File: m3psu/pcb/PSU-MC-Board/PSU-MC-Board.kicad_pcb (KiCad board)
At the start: 2 copper layers, 40 x 40 mm, 60 parts, among them IC1 STM32F405RxTx, IC2 TPS62152, IC3 MCP2562, IC4 LTC4353, IC5 LTC4151, J1 WEST TOP, J2 WEST BOT, J3 NORTH TOP, J4 EAST TOP, J5 EAST BOT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

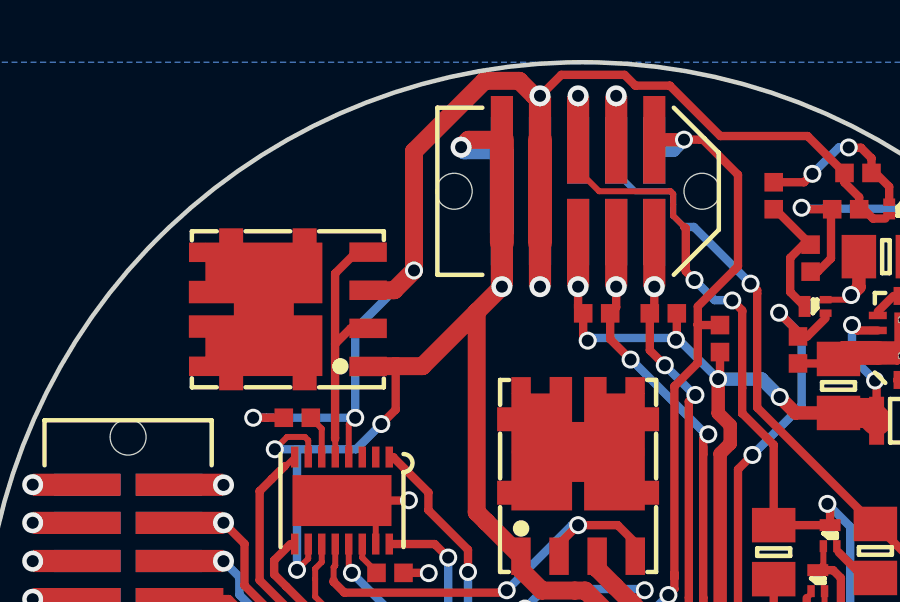
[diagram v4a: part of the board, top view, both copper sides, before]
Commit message: Modified DC-DC board routing to hopefully better performance.
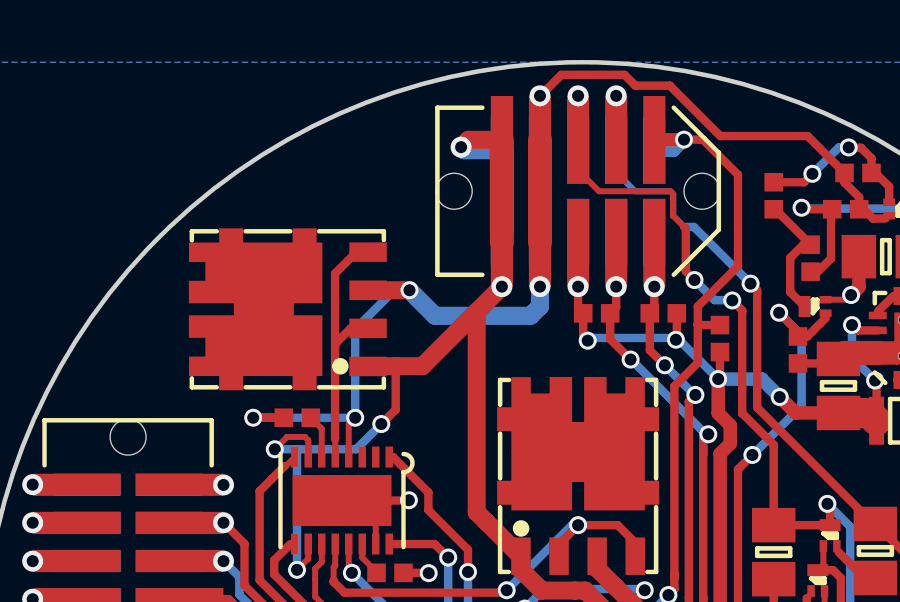
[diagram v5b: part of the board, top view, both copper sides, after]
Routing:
- net VBATT: track 49.6 -> 44.9 mm
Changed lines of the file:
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@@
     (links 240)
     (no_connects 0)
-    (area 80.074999 80.124999 120.225001 120.275001)
+    (area 79.75 79.25 120.225001 120.495)
     (thickness 1.6)
     (drawings 1)
-    (tracks 1171)
+    (tracks 1170)
     (zones 0)
     (modules 60)
@@
   )
   (setup
-    (last_trace_width 0.28)
+    (last_trace_width 0.45)
     (user_trace_width 0.2)
     (user_trace_width 0.28)
@@
   (segment (start 91.455 93.36) (end 91.455 92.415) (width 0.2) (layer F.Cu) (net 13))
   (segment (start 91.455 92.415) (end 91.09 92.05) (width 0.2) (layer F.Cu) (net 13))
-  (via (at 94.53 87.14) (size 0.6) (drill 0.4) (layers F.Cu B.Cu) (net 14))
-  (segment (start 92.57 92.05) (end 92.57 89.1) (width 0.28) (layer B.Cu) (net 14))
-  (segment (start 92.57 89.1) (end 94.53 87.14) (width 0.28) (layer B.Cu) (net 14))
+  (segment (start 94.38 87.8) (end 93.87 87.8) (width 0.28) (layer B.Cu) (net 14))
+  (segment (start 92.57 89.1) (end 92.57 92.05) (width 0.28) (layer B.Cu) (net 14))
+  (segment (start 93.87 87.8) (end 92.57 89.1) (width 0.28) (layer B.Cu) (net 14))
+  (segment (start 98.73 87.68) (end 98.73 88.34) (width 0.6) (layer B.Cu) (net 14))
+  (segment (start 94.38 87.8) (end 93 87.8) (width 0.6) (layer F.Cu) (net 14))
+  (via (at 94.38 87.8) (size 0.6) (drill 0.4) (layers F.Cu B.Cu) (net 14))
+  (segment (start 95.23 88.65) (end 94.38 87.8) (width 0.6) (layer B.Cu) (net 14))
+  (segment (start 98.42 88.65) (end 95.23 88.65) (width 0.6) (layer B.Cu) (net 14))
+  (segment (start 98.73 88.34) (end 98.42 88.65) (width 0.6) (layer B.Cu) (net 14))
   (segment (start 92.355 93.36) (end 92.355 92.265) (width 0.2) (layer F.Cu) (net 14))
-  (segment (start 92.57 92.05) (end 89.62 92.05) (width 0.28) (layer B.Cu) (net 14))
-  (via (at 92.57 92.05) (size 0.6) (drill 0.4) (layers F.Cu B.Cu) (net 14))
   (segment (start 92.355 92.265) (end 92.57 92.05) (width 0.2) (layer F.Cu) (net 14))
-  (segment (start 90.19 92.05) (end 89.17 92.05) (width 0.28) (layer F.Cu) (net 14))
-  (via (at 89.17 92.05) (size 0.6) (drill 0.4) (layers F.Cu B.Cu) (net 14))
+  (via (at 92.57 92.05) (size 0.6) (drill 0.4) (layers F.Cu B.Cu) (net 14))
+  (segment (start 92.57 92.05) (end 89.62 92.05) (width 0.28) (layer B.Cu) (net 14))
   (segment (start 89.62 92.05) (end 89.17 92.05) (width 0.28) (layer B.Cu) (net 14))
-  (segment (start 98.73 81.32) (end 98.54 81.32) (width 0.6) (layer F.Cu) (net 14))
-  (segment (start 94.53 83.17) (end 94.53 87.14) (width 0.6) (layer F.Cu) (net 14))
-  (segment (start 96.88 80.82) (end 94.53 83.17) (width 0.6) (layer F.Cu) (net 14))
-  (segment (start 98.04 80.82) (end 96.88 80.82) (width 0.6) (layer F.Cu) (net 14))
-  (segment (start 98.54 81.32) (end 98.04 80.82) (width 0.6) (layer F.Cu) (net 14))
-  (segment (start 94.53 87.14) (end 93.87 87.8) (width 0.6) (layer F.Cu) (net 14))
-  (segment (start 93.87 87.8) (end 93 87.8) (width 0.6) (layer F.Cu) (net 14))
+  (via (at 89.17 92.05) (size 0.6) (drill 0.4) (layers F.Cu B.Cu) (net 14))
+  (segment (start 90.19 92.05) (end 89.17 92.05) (width 0.28) (layer F.Cu) (net 14))
   (segment (start 98.73 81.32) (end 98.74 81.32) (width 0.28) (layer F.Cu) (net 14))
   (segment (start 107.65 82.66) (end 108.88 83.89) (width 0.28) (layer F.Cu) (net 14))

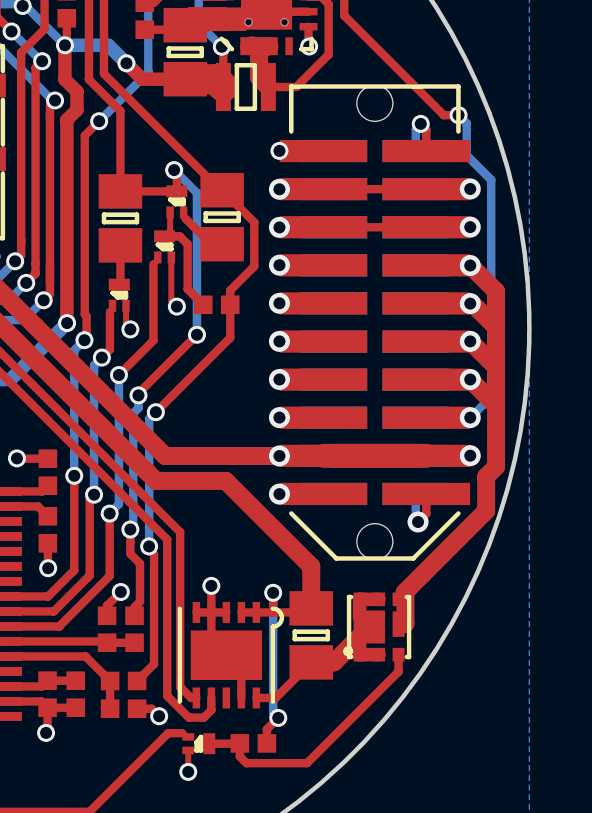
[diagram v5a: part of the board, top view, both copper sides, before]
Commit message: Fix wiring of pyro output from current monitor
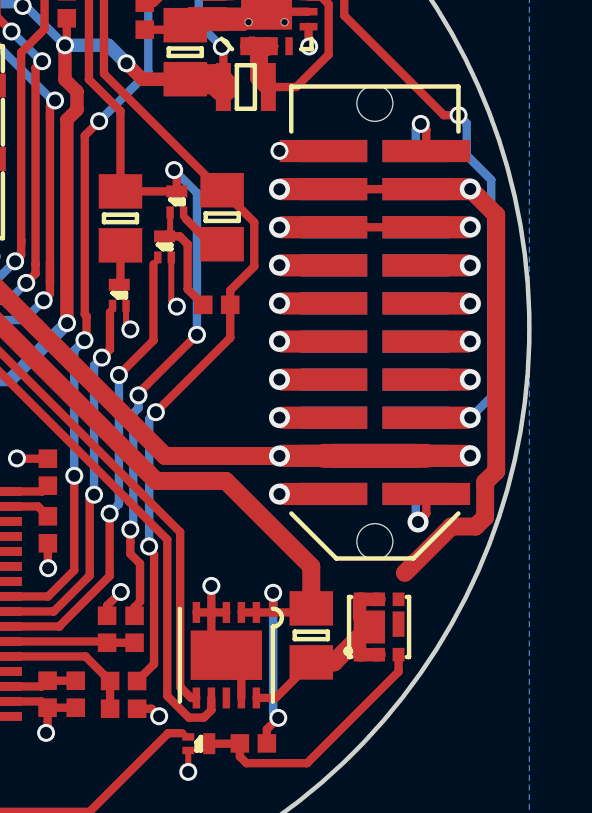
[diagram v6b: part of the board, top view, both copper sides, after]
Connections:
- J4 pad 10: /PYRO1 -> /PYRO2
- J4 pad 12: /PYRO1 -> /PYRO3
- J4 pad 14: /PYRO1 -> /PYRO4
- J5 pad 10: /PYRO1 -> /PYRO2
- J5 pad 12: /PYRO1 -> /PYRO3
- J5 pad 14: /PYRO1 -> /PYRO4
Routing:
- net /PYRO1: track 32.1 -> 3.28 mm, vias 4 -> 1
- net /PYRO_SO: track 10.00 -> 24.9 mm
- net /PYRO2: track 0.00 -> 4.81 mm, vias 0 -> 1
- net /PYRO4: track 0.00 -> 3.29 mm, vias 0 -> 1
- net /PYRO3: track 0.00 -> 3.28 mm, vias 0 -> 1
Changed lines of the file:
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@@
-(kicad_pcb (version 4) (host pcbnew 4.0.0-rc2-stable)
+(kicad_pcb (version 4) (host pcbnew 4.0.0-2.201511301920+6191~38~ubuntu14.04.1-stable)
   (general
-    (links 240)
+    (links 237)
     (no_connects 0)
-    (area 79.75 79.25 120.225001 120.495)
+    (area 80.074999 80.124999 120.225001 120.275001)
     (thickness 1.6)
     (drawings 1)
-    (tracks 1170)
+    (tracks 1160)
     (zones 0)
     (modules 60)
-    (nets 106)
+    (nets 109)
   )
   (page A4)
@@
   )
   (setup
-    (last_trace_width 0.45)
+    (last_trace_width 0.6)
     (user_trace_width 0.2)
     (user_trace_width 0.28)
@@
   (net 104 "Net-(Q7-Pad3)")
   (net 105 "Net-(Q8-Pad1)")
+  (net 106 /PYRO2)
+  (net 107 /PYRO3)
+  (net 108 /PYRO4)
   (net_class Default "This is the default net class."
     (clearance 0.2)
@@
     (add_net /PWR)
     (add_net /PYRO1)
+    (add_net /PYRO2)
+    (add_net /PYRO3)
+    (add_net /PYRO4)
     (add_net /PYRO_SI)
     (add_net /PYRO_SO)
@@
       (net 52 /5v_IMU))
     (pad 10 smd rect (at -0.635 -1.715 270) (size 0.74 2.92) (layers F.Cu F.Paste F.Mask)
-      (net 51 /PYRO1))
+      (net 106 /PYRO2))
     (pad 11 smd rect (at 0.635 1.715 270) (size 0.74 2.92) (layers F.Cu F.Paste F.Mask)
       (net 53 /5v_AUX1))
     (pad 12 smd rect (at 0.635 -1.715 270) (size 0.74 2.92) (layers F.Cu F.Paste F.Mask)
-      (net 51 /PYRO1))
+      (net 107 /PYRO3))
     (pad 13 smd rect (at 1.905 1.715 270) (size 0.74 2.92) (layers F.Cu F.Paste F.Mask)
       (net 54 /5v_AUX2))
     (pad 14 smd rect (at 1.905 -1.715 270) (size 0.74 2.92) (layers F.Cu F.Paste F.Mask)
-      (net 51 /PYRO1))
+      (net 108 /PYRO4))
     (pad 15 smd rect (at 3.175 1.715 270) (size 0.74 2.92) (layers F.Cu F.Paste F.Mask)
       (net 55 /5v_CAM))
@@
       (net 52 /5v_IMU))
     (pad 10 smd rect (at -0.635 -1.365 270) (size 0.74 2.22) (layers B.Cu B.Paste B.Mask)
-      (net 51 /PYRO1))
+      (net 106 /PYRO2))
     (pad 11 smd rect (at 0.635 1.365 270) (size 0.74 2.22) (layers B.Cu B.Paste B.Mask)
       (net 53 /5v_AUX1))
     (pad 12 smd rect (at 0.635 -1.365 270) (size 0.74 2.22) (layers B.Cu B.Paste B.Mask)
-      (net 51 /PYRO1))
+      (net 107 /PYRO3))
     (pad 13 smd rect (at 1.905 1.365 270) (size 0.74 2.22) (layers B.Cu B.Paste B.Mask)
       (net 54 /5v_AUX2))
     (pad 14 smd rect (at 1.905 -1.365 270) (size 0.74 2.22) (layers B.Cu B.Paste B.Mask)
-      (net 51 /PYRO1))
+      (net 108 /PYRO4))
     (pad 15 smd rect (at 3.175 1.365 270) (size 0.74 2.22) (layers B.Cu B.Paste B.Mask)
       (net 55 /5v_CAM))
@@
   (via (at 106.85 100.23) (size 0.6) (drill 0.4) (layers F.Cu B.Cu) (net 0))
   (segment (start 106.705 100.085) (end 106.85 100.23) (width 0.2) (layer F.Cu) (net 0))
+  (segment (start 115.804 110.04) (end 115.79 110.054) (width 0.28) (layer F.Cu) (net 0))
   (via (at 106.531889 108.983222) (size 0.6) (drill 0.4) (layers F.Cu B.Cu) (net 1))
   (segment (start 106.075 109.440111) (end 106.531889 108.983222) (width 0.28) (layer F.Cu) (net 1))
@@
   (segment (start 101.27 81.32) (end 101.27 83.135) (width 0.28) (layer B.Cu) (net 47))
   (via (at 101.27 81.32) (size 0.7) (drill 0.4) (layers F.Cu B.Cu) (net 47))
+  (segment (start 118.360002 106.8) (end 117.548002 106.8) (width 0.6) (layer F.Cu) (net 48))
+  (segment (start 117.548002 106.8) (end 116 108.348002) (width 0.6) (layer F.Cu) (net 48))
+  (segment (start 118.675001 105.324999) (end 118.675001 106.485001) (width 0.6) (layer F.Cu) (net 48))
+  (segment (start 118.675001 106.485001) (end 118.360002 106.8) (width 0.6) (layer F.Cu) (net 48))
+  (segment (start 119.04501 104.95499) (end 118.675001 105.324999) (width 0.6) (layer F.Cu) (net 48))
+  (segment (start 118.18 95.55) (end 119.04501 96.41501) (width 0.6) (layer F.Cu) (net 48))
+  (segment (start 119.04501 96.41501) (end 119.04501 104.95499) (width 0.6) (layer F.Cu) (net 48))
   (segment (start 113.285 95.555) (end 116.715 95.555) (width 0.28) (layer F.Cu) (net 48))
   (segment (start 113.635 95.555) (end 111.825 95.555) (width 0.28) (layer B.Cu) (net 48))
@@
   (segment (start 111.82 98.09) (end 111.825 98.095) (width 0.28) (layer F.Cu) (net 50))
   (segment (start 111.825 98.095) (end 113.285 98.095) (width 0.28) (layer F.Cu) (net 50))
-  (segment (start 116.02 110.04) (end 115.804 110.04) (width 0.28) (layer F.Cu) (net 51))
-  (segment (start 115.804 110.04) (end 115.79 110.054) (width 0.28) (layer F.Cu) (net 51))
-  (segment (start 116.02 108.97) (end 116.02 110.04) (width 0.6) (layer F.Cu) (net 51))
-  (segment (start 116.02 110.04) (end 116.01 110.05) (width 0.6) (layer F.Cu) (net 51))
-  (segment (start 115.99 109) (end 116.02 108.97) (width 0.6) (layer F.Cu) (net 51))
-  (segment (start 116.02 108.97) (end 116.6 108.39) (width 0.6) (layer F.Cu) (net 51))
-  (segment (start 118.71 106.28) (end 116.6 108.39) (width 0.6) (layer F.Cu) (net 51))
-  (segment (start 118.71 105.14) (end 118.71 106.28) (width 0.6) (layer F.Cu) (net 51))
-  (segment (start 119.04 104.81) (end 118.71 105.14) (width 0.6) (layer F.Cu) (net 51))
-  (segment (start 119.04 104.81) (end 119.04 102.77) (width 0.6) (layer F.Cu) (net 51))
-  (segment (start 119.04 101.53) (end 119.04 101.49) (width 0.6) (layer F.Cu) (net 51))
-  (segment (start 119.04 101.49) (end 118.18 100.63) (width 0.6) (layer F.Cu) (net 51))
-  (segment (start 116.715 99.365) (end 118.245 99.365) (width 0.6) (layer F.Cu) (net 51))
-  (segment (start 118.245 99.365) (end 119.04 100.16) (width 0.6) (layer F.Cu) (net 51))
-  (segment (start 119.04 102.77) (end 119.04 101.53) (width 0.6) (layer F.Cu) (net 51))
-  (segment (start 119.04 101.53) (end 119.04 100.16) (width 0.6) (layer F.Cu) (net 51))
-  (segment (start 119.04 100.16) (end 119.04 98.96) (width 0.6) (layer F.Cu) (net 51))
-  (segment (start 119.04 98.96) (end 118.18 98.1) (width 0.6) (layer F.Cu) (net 51))
-  (segment (start 118.18 101.9) (end 118.18 101.91) (width 0.6) (layer F.Cu) (net 51))
-  (segment (start 118.18 101.91) (end 119.04 102.77) (width 0.6) (layer F.Cu) (net 51))
-  (segment (start 116.715 101.905) (end 118.175 101.905) (width 0.28) (layer F.Cu) (net 51))
-  (segment (start 118.175 101.905) (end 118.18 101.9) (width 0.28) (layer F.Cu) (net 51))
-  (via (at 118.18 101.9) (size 0.7) (drill 0.4) (layers F.Cu B.Cu) (net 51))
-  (segment (start 118.18 101.9) (end 118.175 101.905) (width 0.28) (layer B.Cu) (net 51))
-  (segment (start 118.175 101.905) (end 116.365 101.905) (width 0.28) (layer B.Cu) (net 51))
-  (segment (start 116.365 100.635) (end 118.175 100.635) (width 0.28) (layer B.Cu) (net 51))
-  (segment (start 118.175 100.635) (end 118.18 100.63) (width 0.28) (layer B.Cu) (net 51))
-  (via (at 118.18 100.63) (size 0.7) (drill 0.4) (layers F.Cu B.Cu) (net 51))
-  (segment (start 118.18 100.63) (end 118.175 100.635) (width 0.28) (layer F.Cu) (net 51))
-  (segment (start 118.175 100.635) (end 116.715 100.635) (width 0.28) (layer F.Cu) (net 51))
-  (segment (start 116.715 99.365) (end 118.175 99.365) (width 0.28) (layer F.Cu) (net 51))
-  (segment (start 118.175 99.365) (end 118.18 99.37) (width 0.28) (layer F.Cu) (net 51))
-  (via (at 118.18 99.37) (size 0.7) (drill 0.4) (layers F.Cu B.Cu) (net 51))
-  (segment (start 118.18 99.37) (end 118.175 99.365) (width 0.28) (layer B.Cu) (net 51))
-  (segment (start 118.175 99.365) (end 116.365 99.365) (width 0.28) (layer B.Cu) (net 51))
   (segment (start 116.365 98.095) (end 118.175 98.095) (width 0.28) (layer B.Cu) (net 51))
   (segment (start 118.175 98.095) (end 118.18 98.1) (width 0.28) (layer B.Cu) (net 51))
-  (via (at 118.18 98.1) (size 0.7) (drill 0.4) (layers F.Cu B.Cu) (net 51))
   (segment (start 118.18 98.1) (end 118.175 98.095) (width 0.28) (layer F.Cu) (net 51))
   (segment (start 118.175 98.095) (end 116.715 98.095) (width 0.28) (layer F.Cu) (net 51))
+  (via (at 118.18 98.1) (size 0.7) (drill 0.4) (layers F.Cu B.Cu) (net 51))
   (segment (start 113.635 99.365) (end 111.825 99.365) (width 0.28) (layer B.Cu) (net 52))
   (segment (start 111.825 99.365) (end 111.82 99.36) (width 0.28) (layer B.Cu) (net 52))
@@
   (segment (start 112.74 114.69) (end 110.72 114.69) (width 0.28) (layer F.Cu) (net 105))
   (segment (start 115.79 111.64) (end 112.74 114.69) (width 0.28) (layer F.Cu) (net 105))
+  (segment (start 116.715 99.365) (end 118.245 99.365) (width 0.6) (layer F.Cu) (net 106))
+  (segment (start 116.715 99.365) (end 118.175 99.365) (width 0.28) (layer F.Cu) (net 106))
+  (segment (start 118.175 99.365) (end 118.18 99.37) (width 0.28) (layer F.Cu) (net 106))
+  (via (at 118.18 99.37) (size 0.7) (drill 0.4) (layers F.Cu B.Cu) (net 106))
+  (segment (start 118.18 99.37) (end 118.175 99.365) (width 0.28) (layer B.Cu) (net 106))
+  (segment (start 118.175 99.365) (end 116.365 99.365) (width 0.28) (layer B.Cu) (net 106))
+  (via (at 118.18 100.63) (size 0.7) (drill 0.4) (layers F.Cu B.Cu) (net 107))
+  (segment (start 118.175 100.635) (end 118.18 100.63) (width 0.28) (layer B.Cu) (net 107))
+  (segment (start 116.365 100.635) (end 118.175 100.635) (width 0.28) (layer B.Cu) (net 107))
+  (segment (start 118.18 100.63) (end 118.175 100.635) (width 0.28) (layer F.Cu) (net 107))
+  (segment (start 118.175 100.635) (end 116.715 100.635) (width 0.28) (layer F.Cu) (net 107))
+  (segment (start 118.18 101.9) (end 118.18 101.91) (width 0.6) (layer F.Cu) (net 108))
+  (via (at 118.18 101.9) (size 0.7) (drill 0.4) (layers F.Cu B.Cu) (net 108))
+  (segment (start 118.18 101.9) (end 118.175 101.905) (width 0.28) (layer B.Cu) (net 108))
+  (segment (start 116.715 101.905) (end 118.175 101.905) (width 0.28) (layer F.Cu) (net 108))
+  (segment (start 118.175 101.905) (end 118.18 101.9) (width 0.28) (layer F.Cu) (net 108))
+  (segment (start 118.175 101.905) (end 116.365 101.905) (width 0.28) (layer B.Cu) (net 108))
   (zone (net 1) (net_name GND) (layer B.Cu) (hatch edge 0.508)
     (connect_pads (clearance 0.3))
